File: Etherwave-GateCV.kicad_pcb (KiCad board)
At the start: 2 copper layers, 76 parts, among them J1 Etherwave Brd, J2 Volume CV, J3 Pitch CV, J4 Gate, Q1 PMP4501Y, Q2 PMBT3906, Q3 PMP4501Y, U1 LM13700, U2 CD4093, U3 CD4093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

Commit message: about 40 % layout done
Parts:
- U5: footprint Package_SO:TSSOP-8_3x3mm_P0.65mm -> Package_SO:SOIC-8_3.9x4.9mm_P1.27mm
- moved R4 117.4 mm to (68.5, 73.0), turned to -90 degrees
- moved R15 110.1 mm to (69.5, 95.0), turned to 90 degrees
- moved R2 107.0 mm to (71.5, 75.5), turned to 90 degrees
- moved C8 106.2 mm to (72.0, 86.2), turned to 180 degrees
- moved R1 104.5 mm to (68.5, 78.0), turned to 90 degrees
- moved R16 103.9 mm to (68.0, 98.0), turned to 180 degrees
- moved C21 103.9 mm to (88.0, 88.5), turned to 90 degrees
- moved C4 102.2 mm to (69.5, 66.8)
- moved C10 100.6 mm to (69.5, 90.8), turned to 90 degrees
- moved C1 93.7 mm to (71.5, 79.5), turned to -90 degrees
- moved R26 93.4 mm to (89.5, 77.0)
- moved U2 89.6 mm to (77.5, 82.0), turned to -90 degrees
- moved C9 88.7 mm to (72.0, 84.0), turned to 180 degrees
- moved R10 87.0 mm to (79.5, 75.5), turned to -90 degrees
- moved R6 86.9 mm to (75.5, 75.5), turned to -90 degrees
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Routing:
- net +12V: track 0.00 -> 124.9 mm, vias 0 -> 8
- net GND: track 0.00 -> 31.0 mm, vias 0 -> 13
- net Net-(C10-Pad2): track 0.00 -> 23.4 mm
- net Net-(C11-Pad2): track 0.00 -> 17.5 mm, vias 0 -> 2
- net Net-(U2-Pad10): track 0.00 -> 14.4 mm
- net Net-(C1-Pad1): track 0.00 -> 14.2 mm
- net Net-(U2-Pad11): track 0.00 -> 13.8 mm
- net Net-(J1-Pad4): track 0.00 -> 12.3 mm
- net Net-(C4-Pad2): track 0.00 -> 11.5 mm
- net Net-(C9-Pad1): track 0.00 -> 11.3 mm
- net Net-(U2-Pad12): track 0.00 -> 9.78 mm
- net Net-(J1-Pad2): track 0.00 -> 8.68 mm
- net Net-(C4-Pad1): track 0.00 -> 8.64 mm
- net -12V: track 0.00 -> 8.61 mm
- net Net-(R10-Pad2): track 0.00 -> 7.44 mm
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- added copper zone on B.Cu, net GND
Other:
- board outline added: 160 x 100 mm

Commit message: 2/3 of layout
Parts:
- moved J4 107.5 mm to (94.0, 102.7), turned to 180 degrees
- moved J2 99.7 mm to (98.7, 102.8), turned to 0 degrees
- moved J3 89.9 mm to (109.0, 51.2)
- moved R5 79.2 mm to (73.0, 67.2), turned to 90 degrees
- moved R23 79.1 mm to (83.8, 93.0)
- moved R20 79.0 mm to (88.2, 98.2)
- moved R7 78.5 mm to (77.2, 75.5), turned to 90 degrees
- moved R8 77.0 mm to (73.2, 58.8), turned to 180 degrees
- moved R9 74.9 mm to (73.2, 62.2)
- moved R24 68.8 mm to (83.8, 90.0), turned to 180 degrees
- moved C13 61.8 mm to (93.8, 61.5), turned to 90 degrees
- moved RV2 60.2 mm to (119.5, 54.8)
- moved D4 58.5 mm to (88.2, 91.2)
- moved C12 58.3 mm to (78.2, 61.5), turned to 90 degrees
- moved R27 57.5 mm to (90.5, 84.2), turned to 90 degrees
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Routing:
- net -12V: track 8.61 -> 134.4 mm, vias 0 -> 5
- net +12V: track 124.9 -> 199.8 mm, vias 8 -> 14
- net Net-(D4-Pad3): track 0.00 -> 35.5 mm, vias 0 -> 2
- net Net-(C12-Pad1): track 0.00 -> 30.6 mm
- net Net-(C13-Pad1): track 0.00 -> 29.5 mm
- net Net-(Q2-Pad3): track 0.00 -> 27.9 mm
- net GND: track 31.0 -> 57.9 mm, vias 13 -> 24
- net Net-(D1-Pad1): track 0.00 -> 20.0 mm, vias 0 -> 2
- net Net-(Q1-Pad3): track 0.00 -> 16.8 mm
- net Net-(R28-Pad2): track 0.00 -> 11.8 mm
- net Net-(R27-Pad1): track 0.00 -> 11.1 mm
- net Net-(U3-Pad4): track 0.00 -> 8.75 mm
- net Net-(R40-Pad1): track 0.00 -> 8.63 mm
- net Net-(R15-Pad1): track 5.16 -> 13.8 mm
- net Net-(Q1-Pad1): track 0.00 -> 7.33 mm
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
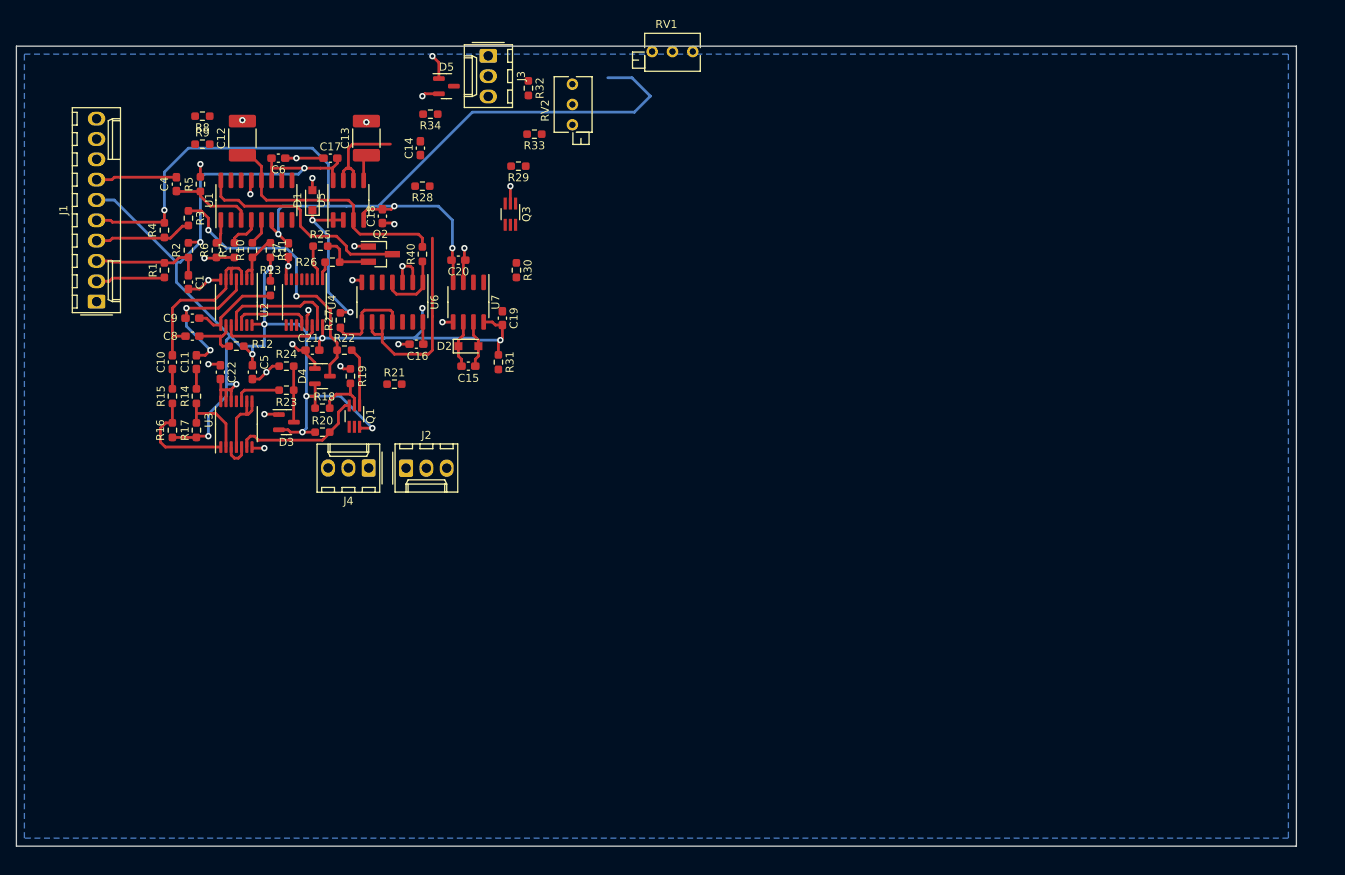
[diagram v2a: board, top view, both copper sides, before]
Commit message: done top layer routing
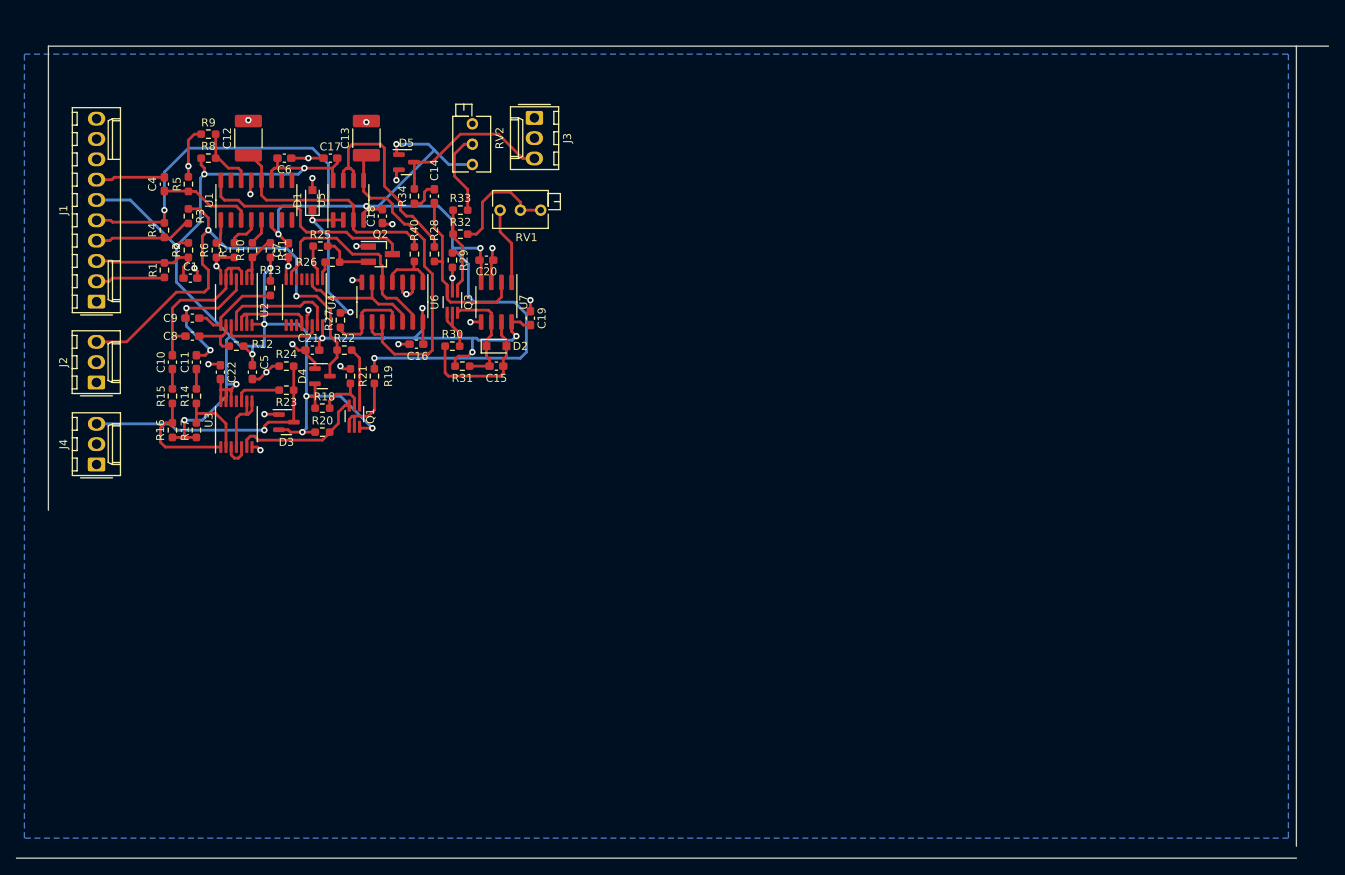
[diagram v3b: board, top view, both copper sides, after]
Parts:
- moved J2 40.2 mm to (60.0, 92.0), turned to 90 degrees
- moved J4 34.0 mm to (60.0, 102.3), turned to 90 degrees
- moved RV1 31.2 mm to (110.5, 70.5), turned to 180 degrees
- moved R32 20.1 mm to (105.5, 73.5), turned to 180 degrees
- moved RV2 16.0 mm to (107.0, 64.8), turned to -90 degrees
- moved R29 14.4 mm to (104.5, 76.8), turned to -90 degrees
- moved R33 13.3 mm to (105.5, 70.5)
- moved Q3 13.2 mm to (104.5, 82.0)
- moved R30 12.4 mm to (104.5, 87.5), turned to 180 degrees
- moved D5 10.7 mm to (98.8, 64.5)
- moved R34 10.4 mm to (99.8, 68.8), turned to -90 degrees
- moved J3 9.66 mm to (114.8, 59.0)
- moved R28 8.63 mm to (102.2, 76.0), turned to 90 degrees
- moved C14 6.25 mm to (102.2, 68.8)
- moved R8 5.30 mm to (74.0, 64.0)
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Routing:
- net Net-(U4-Pad7): track 0.00 -> 26.9 mm
- net Net-(D3-Pad3): track 7.01 -> 32.7 mm, vias 0 -> 1
- net Net-(D4-Pad3): track 35.5 -> 60.3 mm
- net Net-(C14-Pad1): track 0.00 -> 22.7 mm
- net Net-(D5-Pad3): track 0.00 -> 21.1 mm
- net Net-(U4-Pad3): track 0.00 -> 16.5 mm
- net -12V: track 134.4 -> 149.8 mm, vias 5 -> 6
- net Net-(R28-Pad2): track 11.8 -> 26.6 mm
- net Net-(R32-Pad1): track 0.00 -> 14.7 mm
- net Net-(C13-Pad1): track 29.5 -> 41.8 mm
- net Net-(Q3-Pad1): track 0.00 -> 12.2 mm
- net Net-(C15-Pad2): track 5.94 -> 17.8 mm
- net Net-(R33-Pad1): track 0.00 -> 10.5 mm
- net Net-(RV1-Pad1): track 0.00 -> 9.62 mm
- net Net-(Q1-Pad4): track 0.00 -> 9.22 mm
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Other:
- board size 160 x 100 mm -> 164 x 101.5 mm

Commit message: ready for power distribution
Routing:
- net -12V: track 149.8 -> 157.1 mm
- net Net-(D5-Pad3): track 21.1 -> 25.8 mm
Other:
- board size 164 x 101.5 mm -> 67 x 56.5 mm
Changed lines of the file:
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@@
     (property "Sheetname" "")
     (attr through_hole)
-    (fp_text reference "RV2" (at -3.3 -3.41 90) (layer "F.SilkS")
+    (fp_text reference "RV2" (at -3.3 3.25 90) (layer "F.SilkS")
       (effects (font (size 1 1) (thickness 0.15)))
     )
@@
     (property "Sheetname" "")
     (attr through_hole)
-    (fp_text reference "J3" (at 2.54 -4.12 90) (layer "F.SilkS")
+    (fp_text reference "J3" (at -2.46 0 180) (layer "F.SilkS")
       (effects (font (size 1 1) (thickness 0.15)))
     )
@@
     )
   )
-  (gr_line (start 210 151.5) (end 50 151.5) (layer "Edge.Cuts") (width 0.1))
-  (gr_line (start 210 50) (end 210 150) (layer "Edge.Cuts") (width 0.1))
-  (gr_line (start 54 50) (end 214 50) (layer "Edge.Cuts") (width 0.1))
-  (gr_line (start 54 108) (end 54 50) (layer "Edge.Cuts") (width 0.1))
+  (gr_line (start 121 106.5) (end 54 106.5) (layer "Edge.Cuts") (width 0.1))
+  (gr_line (start 121 50) (end 121 106.5) (layer "Edge.Cuts") (width 0.1))
+  (gr_line (start 54 50) (end 121 50) (layer "Edge.Cuts") (width 0.1))
+  (gr_line (start 54 106.5) (end 54 50) (layer "Edge.Cuts") (width 0.1))
   (segment (start 70.3375 76.4125) (end 71.5 76.4125) (width 0.35) (layer "F.Cu") (net 1))
   (segment (start 61.85 76.85) (end 60.02 76.85) (width 0.35) (layer "F.Cu") (net 1))
@@
   (via (at 94.75 89) (size 0.8) (drill 0.4) (layers "F.Cu" "B.Cu") (free) (net 6))
   (via (at 93.75 70) (size 0.8) (drill 0.4) (layers "F.Cu" "B.Cu") (free) (net 6))
+  (segment (start 104.5 75.25) (end 106.5 77.25) (width 0.35) (layer "B.Cu") (net 6))
+  (segment (start 115.5 85.25) (end 115.5 91.5) (width 0.35) (layer "B.Cu") (net 6))
   (segment (start 89 70) (end 91.25 70) (width 0.35) (layer "B.Cu") (net 6))
-  (segment (start 113 89) (end 94.75 89) (width 0.35) (layer "B.Cu") (net 6))
   (segment (start 104.5 75.25) (end 108 75.25) (width 0.35) (layer "B.Cu") (net 6))
   (segment (start 82.75 73.5) (end 82.75 70.5) (width 0.35) (layer "B.Cu") (net 6))
   (segment (start 107 64.79) (end 104.04 64.79) (width 0.35) (layer "B.Cu") (net 6))
-  (segment (start 113.75 83.5) (end 113.75 88.25) (width 0.35) (layer "B.Cu") (net 6))
   (segment (start 82.75 70.5) (end 83.25 70) (width 0.35) (layer "B.Cu") (net 6))
+  (segment (start 114.5 92.5) (end 103.75 92.5) (width 0.35) (layer "B.Cu") (net 6))
+  (segment (start 100.25 89) (end 94.75 89) (width 0.35) (layer "B.Cu") (net 6))
+  (segment (start 87 62.75) (end 71.5 62.75) (width 0.35) (layer "B.Cu") (net 6))
   (segment (start 107.25 82) (end 112.25 82) (width 0.35) (layer "B.Cu") (net 6))
-  (segment (start 112.25 82) (end 113.75 83.5) (width 0.35) (layer "B.Cu") (net 6))
-  (segment (start 87 62.75) (end 71.5 62.75) (width 0.35) (layer "B.Cu") (net 6))
   (segment (start 104.5 71.75) (end 102.75 70) (width 0.35) (layer "B.Cu") (net 6))
   (segment (start 97.5 62.25) (end 101.5 62.25) (width 0.35) (layer "B.Cu") (net 6))
   (segment (start 95.25 70) (end 102.75 70) (width 0.35) (layer "B.Cu") (net 6))
+  (segment (start 102.25 63) (end 95.25 70) (width 0.35) (layer "B.Cu") (net 6))
   (segment (start 106.5 77.25) (end 106.5 81.25) (width 0.35) (layer "B.Cu") (net 6))
-  (segment (start 113.75 88.25) (end 113 89) (width 0.35) (layer "B.Cu") (net 6))
-  (segment (start 102.25 63) (end 95.25 70) (width 0.35) (layer "B.Cu") (net 6))
   (segment (start 83.25 70) (end 89 70) (width 0.35) (layer "B.Cu") (net 6))
   (segment (start 91.25 70) (end 95.25 70) (width 0.35) (layer "B.Cu") (net 6))
   (segment (start 104.04 64.79) (end 102.25 63) (width 0.35) (layer "B.Cu") (net 6))
-  (segment (start 106.5 81.25) (end 107.25 82) (width 0.35) (layer "B.Cu") (net 6))
+  (segment (start 115.5 91.5) (end 114.5 92.5) (width 0.35) (layer "B.Cu") (net 6))
   (segment (start 89 64.75) (end 87 62.75) (width 0.35) (layer "B.Cu") (net 6))
-  (segment (start 104.5 75.25) (end 106.5 77.25) (width 0.35) (layer "B.Cu") (net 6))
   (segment (start 101.5 62.25) (end 102.25 63) (width 0.35) (layer "B.Cu") (net 6))
   (segment (start 68.5 65.75) (end 68.5 70.5) (width 0.35) (layer "B.Cu") (net 6))
   (segment (start 104.5 75.25) (end 104.5 71.75) (width 0.35) (layer "B.Cu") (net 6))
   (segment (start 89 70) (end 89 64.75) (width 0.35) (layer "B.Cu") (net 6))
+  (segment (start 106.5 81.25) (end 107.25 82) (width 0.35) (layer "B.Cu") (net 6))
   (segment (start 71.5 62.75) (end 68.5 65.75) (width 0.35) (layer "B.Cu") (net 6))
+  (segment (start 103.75 92.5) (end 100.25 89) (width 0.35) (layer "B.Cu") (net 6))
+  (segment (start 112.25 82) (end 115.5 85.25) (width 0.35) (layer "B.Cu") (net 6))
   (segment (start 75.75 86.25) (end 76.2 85.8) (width 0.35) (layer "F.Cu") (net 7))
   (segment (start 75.75 87.5) (end 75.5 87.25) (width 0.35) (layer "F.Cu") (net 7))
@@
   (segment (start 76.25 75.25) (end 74 73) (width 0.35) (layer "B.Cu") (net 21))
   (segment (start 85 81.25) (end 85 76.5) (width 0.35) (layer "B.Cu") (net 21))
-  (segment (start 99.6875 64.5) (end 102 64.5) (width 0.35) (layer "F.Cu") (net 22))
   (segment (start 99.75 66.5) (end 99.75 64.5625) (width 0.35) (layer "F.Cu") (net 22))
+  (segment (start 113.29 64.04) (end 110.25 61) (width 0.35) (layer "F.Cu") (net 22))
+  (segment (start 108.5 57.5) (end 105.5 57.5) (width 0.35) (layer "F.Cu") (net 22))
   (segment (start 99.75 64.5625) (end 99.6875 64.5) (width 0.35) (layer "F.Cu") (net 22))
-  (segment (start 102 64.5) (end 105.5 61) (width 0.35) (layer "F.Cu") (net 22))
-  (segment (start 105.5 61) (end 110.25 61) (width 0.35) (layer "F.Cu") (net 22))
+  (segment (start 105.5 57.5) (end 99.6875 63.3125) (width 0.35) (layer "F.Cu") (net 22))
+  (segment (start 114.75 64.04) (end 113.29 64.04) (width 0.35) (layer "F.Cu") (net 22))
+  (segment (start 110.25 61) (end 110.25 59.25) (width 0.35) (layer "F.Cu") (net 22))
   (segment (start 99.75 67.8375) (end 99.75 66.5) (width 0.35) (layer "F.Cu") (net 22))
-  (segment (start 113.29 64.04) (end 114.75 64.04) (width 0.35) (layer "F.Cu") (net 22))
-  (segment (start 110.25 61) (end 113.29 64.04) (width 0.35) (layer "F.Cu") (net 22))
+  (segment (start 99.6875 63.3125) (end 99.6875 64.5) (width 0.35) (layer "F.Cu") (net 22))
+  (segment (start 110.25 59.25) (end 108.5 57.5) (width 0.35) (layer "F.Cu") (net 22))
   (segment (start 68.25 79) (end 62 79) (width 0.35) (layer "F.Cu") (net 23))
   (segment (start 62 79) (end 61.61 79.39) (width 0.35) (layer "F.Cu") (net 23))
@@
   (segment (start 90.4625 76.95) (end 90.4125 77) (width 0.35) (layer "F.Cu") (net 35))
   (segment (start 94 76.95) (end 90.4625 76.95) (width 0.35) (layer "F.Cu") (net 35))
+  (segment (start 85.5 72.5) (end 85.5 70.5) (width 0.35) (layer "F.Cu") (net 36))
   (segment (start 97 74.75) (end 96.25 74) (width 0.35) (layer "F.Cu") (net 36))
+  (segment (start 85.5 70.5) (end 85 70) (width 0.35) (layer "F.Cu") (net 36))
   (segment (start 91.25 73.25) (end 86.25 73.25) (width 0.35) (layer "F.Cu") (net 36))
+  (segment (start 75.555 68.805) (end 75.555 66.775) (width 0.35) (layer "F.Cu") (net 36))
+  (segment (start 85 70) (end 78.75 70) (width 0.35) (layer "F.Cu") (net 36))
+  (segment (start 97 76) (end 97 74.75) (width 0.35) (layer "F.Cu") (net 36))
+  (segment (start 76 69.25) (end 75.555 68.805) (width 0.35) (layer "F.Cu") (net 36))
+  (segment (start 96.25 74) (end 92 74) (width 0.35) (layer "F.Cu") (net 36))
+  (segment (start 86.25 73.25) (end 85.5 72.5) (width 0.35) (layer "F.Cu") (net 36))
   (segment (start 92 74) (end 91.25 73.25) (width 0.35) (layer "F.Cu") (net 36))
-  (segment (start 85 70) (end 78.5 70) (width 0.35) (layer "F.Cu") (net 36))
-  (segment (start 75.555 68.805) (end 75.555 66.775) (width 0.35) (layer "F.Cu") (net 36))
-  (segment (start 76 69.25) (end 75.555 68.805) (width 0.35) (layer "F.Cu") (net 36))
-  (segment (start 97 76) (end 97 74.75) (width 0.35) (layer "F.Cu") (net 36))
-  (segment (start 77.75 69.25) (end 76 69.25) (width 0.35) (layer "F.Cu") (net 36))
-  (segment (start 86.25 73.25) (end 85.5 72.5) (width 0.35) (layer "F.Cu") (net 36))
-  (segment (start 85.5 70.5) (end 85 70) (width 0.35) (layer "F.Cu") (net 36))
-  (segment (start 78.5 70) (end 77.75 69.25) (width 0.35) (layer "F.Cu") (net 36))
-  (segment (start 96.25 74) (end 92 74) (width 0.35) (layer "F.Cu") (net 36))
-  (segment (start 85.5 72.5) (end 85.5 70.5) (width 0.35) (layer "F.Cu") (net 36))
+  (segment (start 78 69.25) (end 76 69.25) (width 0.35) (layer "F.Cu") (net 36))
+  (segment (start 78.75 70) (end 78 69.25) (width 0.35) (layer "F.Cu") (net 36))
   (segment (start 104.5 75.8375) (end 105.6625 75.8375) (width 0.35) (layer "F.Cu") (net 37))
   (segment (start 105.75 75) (end 104.5875 73.8375) (width 0.35) (layer "F.Cu") (net 37))
@@
     (polygon
       (pts
-        (xy 209 149)
-        (xy 51 149)
-        (xy 51 51)
-        (xy 209 51)
+        (xy 120.5 106)
+        (xy 54.5 106)
+        (xy 54.5 50.5)
+        (xy 120.5 50.5)
       )
     )

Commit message: -12 routing done, part of +12 V
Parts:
- moved D5 2.25 mm to (101.0, 64.5)
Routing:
- net +12V: track 209.0 -> 273.2 mm, vias 16 -> 17
- net -12V: track 157.1 -> 110.0 mm, vias 6 -> 9
- net Net-(D3-Pad3): track 32.7 -> 33.7 mm, vias 1 -> 2
- net Net-(D4-Pad3): track 60.3 -> 59.4 mm
- net GND: track 60.2 -> 60.3 mm, vias 25 -> 26
